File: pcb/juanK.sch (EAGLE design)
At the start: 83 parts, among them IC1 MEGA8-P, IC2 7805TV, T1 2N3904, T2 TIC106S, T3 TIC106S, T4 TIC106S, T5 TIC106S, T6 TIC106S, T7 TIC106S

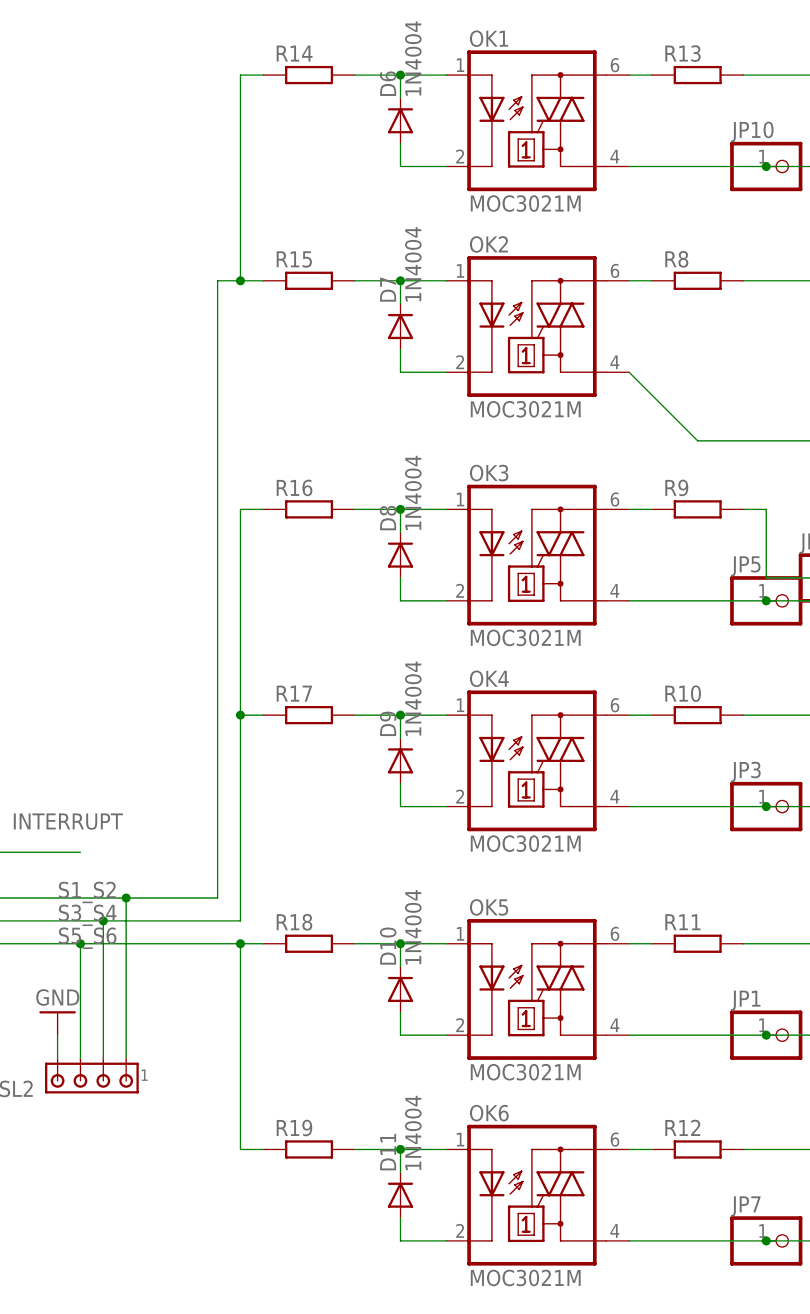
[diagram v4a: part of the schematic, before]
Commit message: Corregir conexión de tierra en los MOC
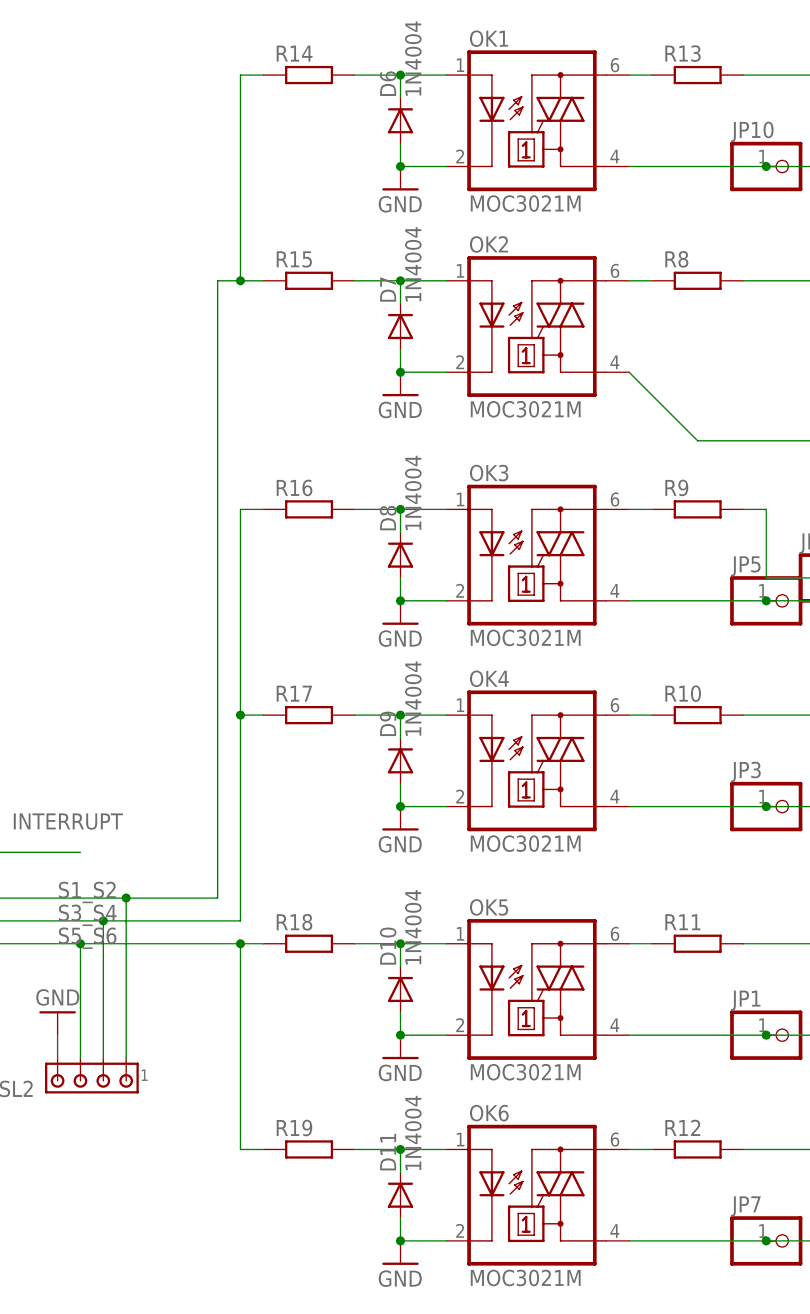
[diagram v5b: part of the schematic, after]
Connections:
- removed net N$29: D6.A, OK1.C
- removed net N$31: D7.A, OK2.C
- removed net N$33: D8.A, OK3.C
- removed net N$34: D9.A, OK4.C
- removed net N$38: D11.A, OK6.C
- removed net N$39: D10.A, OK5.C
- net GND: now also D10.A, D11.A, D6.A, D7.A, D8.A, D9.A, OK1.C, OK2.C, OK3.C, OK4.C, OK5.C, OK6.C
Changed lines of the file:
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@@
 <classes>
 <class number="0" name="default" width="0.508" drill="0.508">
-<clearance class="0" value="1.016"/>
+<clearance class="0" value="0.889"/>
 </class>
 <class number="1" name="power" width="0.762" drill="0.762">
@@
 <part name="R20" library="rcl" deviceset="R-EU_" device="0204/5"/>
 <part name="GND11" library="supply1" deviceset="GND" device=""/>
+<part name="GND12" library="supply1" deviceset="GND" device=""/>
+<part name="GND13" library="supply1" deviceset="GND" device=""/>
+<part name="GND14" library="supply1" deviceset="GND" device=""/>
+<part name="GND15" library="supply1" deviceset="GND" device=""/>
+<part name="GND16" library="supply1" deviceset="GND" device=""/>
+<part name="GND17" library="supply1" deviceset="GND" device=""/>
 </parts>
 <sheets>
@@
 <instance part="R20" gate="G$1" x="-139.7" y="91.44" rot="R90"/>
 <instance part="GND11" gate="1" x="-139.7" y="71.12"/>
+<instance part="GND12" gate="1" x="43.18" y="10.16"/>
+<instance part="GND13" gate="1" x="43.18" y="-12.7"/>
+<instance part="GND14" gate="1" x="43.18" y="35.56"/>
+<instance part="GND15" gate="1" x="43.18" y="58.42"/>
+<instance part="GND16" gate="1" x="43.18" y="106.68"/>
+<instance part="GND17" gate="1" x="43.18" y="83.82"/>
 </instances>
 <busses>
@@
 <pinref part="GND11" gate="1" pin="GND"/>
 <wire x1="-139.7" y1="73.66" x2="-139.7" y2="76.2" width="0.1524" layer="91"/>
+</segment>
+<segment>
+<pinref part="D10" gate="1" pin="A"/>
+<pinref part="OK5" gate="-1" pin="C"/>
+<wire x1="43.18" y1="15.24" x2="43.18" y2="12.7" width="0.1524" layer="91"/>
+<wire x1="43.18" y1="12.7" x2="48.26" y2="12.7" width="0.1524" layer="91"/>
+<pinref part="GND12" gate="1" pin="GND"/>
+<junction x="43.18" y="12.7"/>
+</segment>
+<segment>
+<pinref part="D11" gate="1" pin="A"/>
+<wire x1="43.18" y1="-7.62" x2="43.18" y2="-10.16" width="0.1524" layer="91"/>
+<pinref part="OK6" gate="-1" pin="C"/>
+<wire x1="43.18" y1="-10.16" x2="48.26" y2="-10.16" width="0.1524" layer="91"/>
+<pinref part="GND13" gate="1" pin="GND"/>
+<junction x="43.18" y="-10.16"/>
+</segment>
+<segment>
+<pinref part="D9" gate="1" pin="A"/>
+<wire x1="43.18" y1="40.64" x2="43.18" y2="38.1" width="0.1524" layer="91"/>
+<pinref part="OK4" gate="-1" pin="C"/>
+<wire x1="43.18" y1="38.1" x2="48.26" y2="38.1" width="0.1524" layer="91"/>
+<pinref part="GND14" gate="1" pin="GND"/>
+<junction x="43.18" y="38.1"/>
+</segment>
+<segment>
+<pinref part="D8" gate="1" pin="A"/>
+<wire x1="43.18" y1="63.5" x2="43.18" y2="60.96" width="0.1524" layer="91"/>
+<pinref part="OK3" gate="-1" pin="C"/>
+<wire x1="43.18" y1="60.96" x2="48.26" y2="60.96" width="0.1524" layer="91"/>
+<pinref part="GND15" gate="1" pin="GND"/>
+<junction x="43.18" y="60.96"/>
+</segment>
+<segment>
+<pinref part="D6" gate="1" pin="A"/>
+<wire x1="43.18" y1="111.76" x2="43.18" y2="109.22" width="0.1524" layer="91"/>
+<pinref part="OK1" gate="-1" pin="C"/>
+<wire x1="43.18" y1="109.22" x2="48.26" y2="109.22" width="0.1524" layer="91"/>
+<pinref part="GND16" gate="1" pin="GND"/>
+<junction x="43.18" y="109.22"/>
+</segment>
+<segment>
+<pinref part="D7" gate="1" pin="A"/>
+<wire x1="43.18" y1="88.9" x2="43.18" y2="86.36" width="0.1524" layer="91"/>
+<pinref part="OK2" gate="-1" pin="C"/>
+<wire x1="43.18" y1="86.36" x2="48.26" y2="86.36" width="0.1524" layer="91"/>
+<pinref part="GND17" gate="1" pin="GND"/>
+<junction x="43.18" y="86.36"/>
 </segment>
 </net>
@@
 </segment>
 </net>
-<net name="N$29" class="0">
-<segment>
-<pinref part="D6" gate="1" pin="A"/>
-<wire x1="43.18" y1="111.76" x2="43.18" y2="109.22" width="0.1524" layer="91"/>
-<pinref part="OK1" gate="-1" pin="C"/>
-<wire x1="43.18" y1="109.22" x2="48.26" y2="109.22" width="0.1524" layer="91"/>
-</segment>
-</net>
 <net name="N$30" class="0">
 <segment>
@@
 </segment>
 </net>
-<net name="N$31" class="0">
-<segment>
-<pinref part="D7" gate="1" pin="A"/>
-<wire x1="43.18" y1="88.9" x2="43.18" y2="86.36" width="0.1524" layer="91"/>
-<pinref part="OK2" gate="-1" pin="C"/>
-<wire x1="43.18" y1="86.36" x2="48.26" y2="86.36" width="0.1524" layer="91"/>
-</segment>
-</net>
 <net name="N$32" class="0">
 <segment>
@@
 </segment>
 </net>
-<net name="N$33" class="0">
-<segment>
-<pinref part="D8" gate="1" pin="A"/>
-<wire x1="43.18" y1="63.5" x2="43.18" y2="60.96" width="0.1524" layer="91"/>
-<pinref part="OK3" gate="-1" pin="C"/>
-<wire x1="43.18" y1="60.96" x2="48.26" y2="60.96" width="0.1524" layer="91"/>
-</segment>
-</net>
-<net name="N$34" class="0">
-<segment>
-<pinref part="D9" gate="1" pin="A"/>
-<wire x1="43.18" y1="40.64" x2="43.18" y2="38.1" width="0.1524" layer="91"/>
-<pinref part="OK4" gate="-1" pin="C"/>
-<wire x1="43.18" y1="38.1" x2="48.26" y2="38.1" width="0.1524" layer="91"/>
-</segment>
-</net>
 <net name="N$35" class="0">
 <segment>
@@
 </segment>
 </net>
-<net name="N$38" class="0">
-<segment>
-<pinref part="D11" gate="1" pin="A"/>
-<wire x1="43.18" y1="-7.62" x2="43.18" y2="-10.16" width="0.1524" layer="91"/>
-<pinref part="OK6" gate="-1" pin="C"/>
-<wire x1="43.18" y1="-10.16" x2="48.26" y2="-10.16" width="0.1524" layer="91"/>
-</segment>
-</net>
-<net name="N$39" class="0">
-<segment>
-<pinref part="D10" gate="1" pin="A"/>
-<pinref part="OK5" gate="-1" pin="C"/>
-<wire x1="43.18" y1="15.24" x2="43.18" y2="12.7" width="0.1524" layer="91"/>
-<wire x1="43.18" y1="12.7" x2="48.26" y2="12.7" width="0.1524" layer="91"/>
-</segment>
-</net>
